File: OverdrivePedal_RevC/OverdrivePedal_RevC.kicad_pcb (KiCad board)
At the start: 2 copper layers, 42.5 x 30.5 mm, 58 parts, among them J1 AudioJack2-Connector, J2 Barrel_Jack, J3 Conn_01x05, J4 SW_SPST, J6 AudioJack2-Connector, U1 DG468DV_T1_E3, U10 PAM2812, U2 TL071, U3 TPS60400, U4 DG468DV_T1_E3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

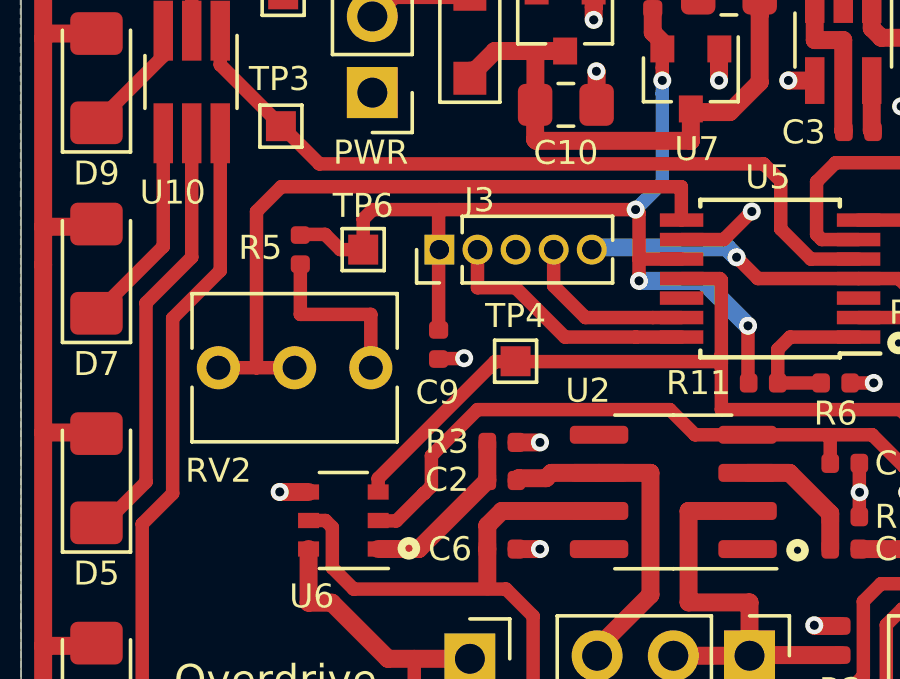
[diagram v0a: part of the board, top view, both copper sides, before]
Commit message: fixed wiring mistake on trim pot
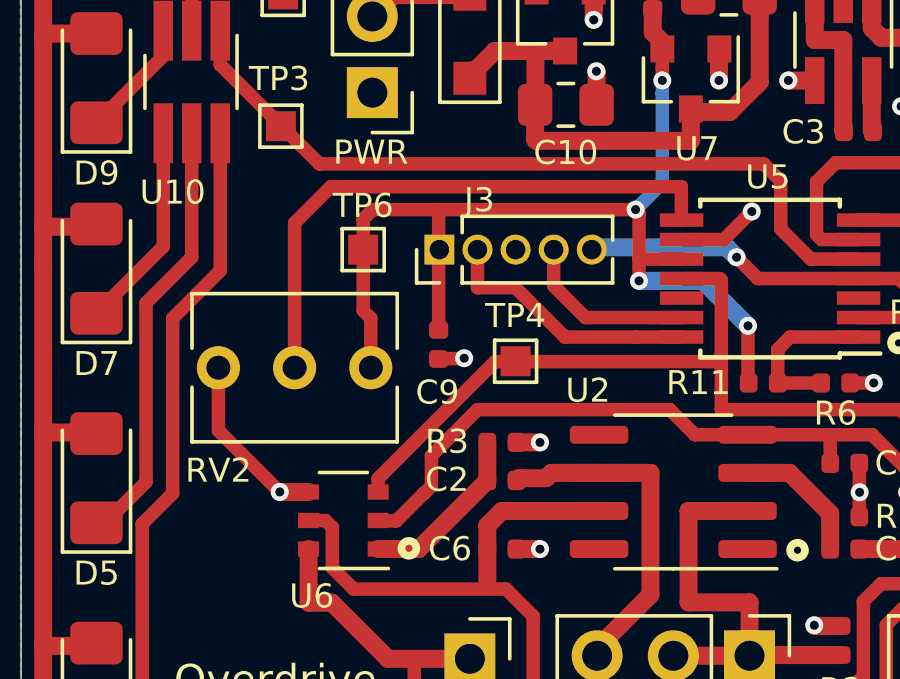
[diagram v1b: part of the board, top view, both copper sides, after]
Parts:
- removed R5: 1K, Resistor_SMD:R_0402_1005Metric
- C1, C2: value C -> 10uF
- R1: value 22M -> 10M
- R3: value 10K -> 10M
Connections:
- RV1 pad 3: Net-(C2-Pad2) -> Net-(R9-Pad2)
- RV2 pad 1: Net-(RV2-Pad1) -> GNDS
- RV2 pad 2: Net-(RV2-Pad1) -> Net-(RV2-Pad2)
- RV2 pad 3: Net-(R5-Pad1) -> +3V3
- U5 pad 8: Net-(RV2-Pad1) -> Net-(RV2-Pad2)
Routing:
- net Net-(RV2-Pad1): track 23.4 -> 0.00 mm
- net Net-(RV2-Pad2): track 0.00 -> 19.3 mm
- net Net-(R5-Pad1): track 5.80 -> 0.00 mm
- net GNDS: track 31.2 -> 36.2 mm
- net +3V3: track 33.5 -> 35.3 mm
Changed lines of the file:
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@@
     (thickness 1.6)
     (drawings 17)
-    (tracks 405)
+    (tracks 401)
     (zones 0)
-    (modules 58)
+    (modules 57)
     (nets 41)
   )
@@
   )
   (setup
-    (last_trace_width 0.25)
+    (last_trace_width 0.45)
     (user_trace_width 0.45)
     (user_trace_width 0.6)
@@
   (net 37 "Net-(U5-Pad12)")
   (net 38 "Net-(U5-Pad3)")
-  (net 39 "Net-(R5-Pad1)")
-  (net 40 "Net-(RV2-Pad1)")
+  (net 39 "Net-(R9-Pad2)")
+  (net 40 "Net-(RV2-Pad2)")
   (net_class Default "This is the default net class."
     (clearance 0.2)
@@
     (add_net "Net-(R11-Pad2)")
     (add_net "Net-(R2-Pad1)")
-    (add_net "Net-(R5-Pad1)")
-    (add_net "Net-(RV2-Pad1)")
+    (add_net "Net-(R9-Pad2)")
+    (add_net "Net-(RV2-Pad2)")
     (add_net "Net-(U2-Pad1)")
     (add_net "Net-(U2-Pad5)")
@@
     (fp_line (start 2.35 -0.76) (end 2.35 5.84) (layer F.Fab) (width 0.1))
     (pad 1 thru_hole circle (at 0 0 90) (size 1.44 1.44) (drill 0.8) (layers *.Cu *.Mask)
-      (net 40 "Net-(RV2-Pad1)"))
+      (net 1 GNDS))
     (pad 2 thru_hole circle (at 0 2.54 90) (size 1.44 1.44) (drill 0.8) (layers *.Cu *.Mask)
-      (net 40 "Net-(RV2-Pad1)"))
+      (net 40 "Net-(RV2-Pad2)"))
     (pad 3 thru_hole circle (at 0 5.08 90) (size 1.44 1.44) (drill 0.8) (layers *.Cu *.Mask)
-      (net 39 "Net-(R5-Pad1)"))
+      (net 20 +3V3))
     (model ${KISYS3DMOD}/Potentiometer_THT.3dshapes/Potentiometer_Vishay_T73XW_Horizontal.wrl
-      (at (xyz 0 0 0))
-      (scale (xyz 1 1 1))
-      (rotate (xyz 0 0 0))
-    )
-  )
-  (module Resistor_SMD:R_0402_1005Metric (layer F.Cu)
-    (at 132.5245 91.44 90)
-    (descr "Resistor SMD 0402 (1005 Metric), square (rectangular) end terminal, IPC_7351 nominal, (Body size source: http://www.tortai-tech.com/upload/download/2011102023233369053.pdf), generated with kicad-footprint-generator")
-    (tags resistor)
-    (attr smd)
-    (fp_text reference R5 (at 0.0635 -1.3335 180) (layer F.SilkS)
-      (effects (font (size 0.8 0.8) (thickness 0.15)))
-    )
-    (fp_text value 1K (at 0 1.17 90) (layer F.Fab)
-      (effects (font (size 1 1) (thickness 0.15)))
-    )
-    (fp_text user %R (at 0 0 90) (layer F.Fab)
-      (effects (font (size 1 1) (thickness 0.15)))
-    )
-    (fp_line (start 0.93 0.47) (end -0.93 0.47) (layer F.CrtYd) (width 0.05))
-    (fp_line (start 0.93 -0.47) (end 0.93 0.47) (layer F.CrtYd) (width 0.05))
-    (fp_line (start -0.93 -0.47) (end 0.93 -0.47) (layer F.CrtYd) (width 0.05))
-    (fp_line (start -0.93 0.47) (end -0.93 -0.47) (layer F.CrtYd) (width 0.05))
-    (fp_line (start 0.5 0.25) (end -0.5 0.25) (layer F.Fab) (width 0.1))
-    (fp_line (start 0.5 -0.25) (end 0.5 0.25) (layer F.Fab) (width 0.1))
-    (fp_line (start -0.5 -0.25) (end 0.5 -0.25) (layer F.Fab) (width 0.1))
-    (fp_line (start -0.5 0.25) (end -0.5 -0.25) (layer F.Fab) (width 0.1))
-    (pad 2 smd roundrect (at 0.485 0 90) (size 0.59 0.64) (layers F.Cu F.Paste F.Mask) (roundrect_rratio 0.25)
-      (net 20 +3V3))
-    (pad 1 smd roundrect (at -0.485 0 90) (size 0.59 0.64) (layers F.Cu F.Paste F.Mask) (roundrect_rratio 0.25)
-      (net 39 "Net-(R5-Pad1)"))
-    (model ${KISYS3DMOD}/Resistor_SMD.3dshapes/R_0402_1005Metric.wrl
       (at (xyz 0 0 0))
       (scale (xyz 1 1 1))
@@
       (net 1 GNDS))
     (pad 8 smd rect (at 2.95 1.95 180) (size 1.45 0.45) (layers F.Cu F.Paste F.Mask)
-      (net 40 "Net-(RV2-Pad1)"))
+      (net 40 "Net-(RV2-Pad2)"))
     (pad 7 smd rect (at -2.95 1.95 180) (size 1.45 0.45) (layers F.Cu F.Paste F.Mask)
       (net 31 /GPIO_EXTI4_BYPASS))
@@
     (fp_line (start -0.635 -1.27) (end 1.27 -1.27) (layer F.Fab) (width 0.1))
     (pad 3 thru_hole oval (at 0 5.08 270) (size 1.7 1.7) (drill 1) (layers *.Cu *.Mask)
-      (net 8 "Net-(C2-Pad2)"))
+      (net 39 "Net-(R9-Pad2)"))
     (pad 2 thru_hole oval (at 0 2.54 270) (size 1.7 1.7) (drill 1) (layers *.Cu *.Mask)
       (net 16 "Net-(R2-Pad1)"))
@@
       (effects (font (size 0.8 0.8) (thickness 0.15)))
     )
-    (fp_text value 10K (at 0 1.17) (layer F.Fab)
+    (fp_text value 10M (at 0 1.17) (layer F.Fab)
       (effects (font (size 1 1) (thickness 0.15)))
     )
@@
       (effects (font (size 0.8 0.8) (thickness 0.15)))
     )
-    (fp_text value 22M (at 0 1.17) (layer F.Fab)
+    (fp_text value 10M (at 0 1.17) (layer F.Fab)
       (effects (font (size 1 1) (thickness 0.15)))
     )
@@
       (effects (font (size 0.8 0.8) (thickness 0.15)))
     )
-    (fp_text value C (at 0 1.17) (layer F.Fab)
+    (fp_text value 10uF (at 0 1.17) (layer F.Fab)
       (effects (font (size 1 1) (thickness 0.15)))
     )
@@
       (effects (font (size 0.8 0.8) (thickness 0.15)))
     )
-    (fp_text value C (at 0 1.17) (layer F.Fab)
+    (fp_text value 10uF (at 0 1.17) (layer F.Fab)
       (effects (font (size 1 1) (thickness 0.15)))
     )
@@
   (via (at 137.9855 95.0595) (size 0.6) (drill 0.3) (layers F.Cu B.Cu) (net 1))
   (segment (start 137.1497 95.0722) (end 137.9728 95.0722) (width 0.45) (layer F.Cu) (net 1))
+  (segment (start 129.794 97.4725) (end 131.8387 99.5172) (width 0.45) (layer F.Cu) (net 1))
+  (segment (start 129.794 95.377) (end 129.794 97.4725) (width 0.45) (layer F.Cu) (net 1))
   (segment (start 141.374 84.843) (end 141.351 84.82) (width 0.6) (layer F.Cu) (net 2))
   (segment (start 139.0048 84.82) (end 141.351 84.82) (width 0.6) (layer F.Cu) (net 2))
@@
   (segment (start 147.447 93.98) (end 147.447 95.862) (width 0.45) (layer F.Cu) (net 20))
   (segment (start 137.414 91.186) (end 137.16 91.44) (width 0.45) (layer F.Cu) (net 20))
-  (segment (start 133.858 91.44) (end 133.35 90.932) (width 0.45) (layer F.Cu) (net 20))
-  (segment (start 134.62 91.44) (end 133.858 91.44) (width 0.45) (layer F.Cu) (net 20))
-  (segment (start 132.5475 90.932) (end 132.5245 90.955) (width 0.45) (layer F.Cu) (net 20))
-  (segment (start 133.35 90.932) (end 132.5475 90.932) (width 0.45) (layer F.Cu) (net 20))
   (segment (start 143.7005 90.1065) (end 144.5895 89.2175) (width 0.45) (layer B.Cu) (net 20))
   (segment (start 144.5895 86.225464) (end 144.5895 85.8012) (width 0.45) (layer B.Cu) (net 20))
@@
   (segment (start 137.1346 90.1319) (end 137.16 90.1065) (width 0.45) (layer F.Cu) (net 20))
   (segment (start 137.1346 94.1173) (end 137.1346 90.1319) (width 0.45) (layer F.Cu) (net 20))
+  (segment (start 134.874 95.377) (end 134.874 93.726) (width 0.45) (layer F.Cu) (net 20))
+  (segment (start 134.62 93.472) (end 134.62 91.44) (width 0.45) (layer F.Cu) (net 20))
+  (segment (start 134.874 93.726) (end 134.62 93.472) (width 0.45) (layer F.Cu) (net 20))
   (segment (start 161.4932 91.8607) (end 163.195 93.5625) (width 0.45) (layer F.Cu) (net 21))
   (segment (start 161.4932 90.043) (end 161.4932 91.8607) (width 0.45) (layer F.Cu) (net 21))
@@
   (segment (start 148.8498 94.3552) (end 148.44 94.765) (width 0.45) (layer F.Cu) (net 36))
   (segment (start 148.44 95.885) (end 149.883 95.885) (width 0.45) (layer F.Cu) (net 36))
-  (segment (start 134.874 95.377) (end 134.874 93.599) (width 0.45) (layer F.Cu) (net 39))
-  (segment (start 134.874 93.599) (end 132.5245 93.599) (width 0.45) (layer F.Cu) (net 39))
-  (segment (start 132.5245 93.599) (end 132.5245 91.925) (width 0.45) (layer F.Cu) (net 39))
-  (segment (start 131.064 95.377) (end 131.064 90.17) (width 0.45) (layer F.Cu) (net 40))
-  (segment (start 131.064 95.377) (end 129.794 95.377) (width 0.45) (layer F.Cu) (net 40))
-  (segment (start 132.334 95.377) (end 131.064 95.377) (width 0.45) (layer F.Cu) (net 40))
-  (segment (start 131.064 90.17) (end 131.8895 89.3445) (width 0.45) (layer F.Cu) (net 40))
-  (segment (start 131.8895 89.3445) (end 145.2245 89.3445) (width 0.45) (layer F.Cu) (net 40))
-  (segment (start 145.2245 90.4461) (end 145.2336 90.4552) (width 0.45) (layer F.Cu) (net 40))
-  (segment (start 145.2245 89.3445) (end 145.2245 90.4461) (width 0.45) (layer F.Cu) (net 40))
+  (segment (start 132.334 90.551) (end 132.334 95.377) (width 0.45) (layer F.Cu) (net 40))
+  (segment (start 133.5405 89.3445) (end 132.334 90.551) (width 0.45) (layer F.Cu) (net 40))
+  (segment (start 145.2245 89.3445) (end 133.5405 89.3445) (width 0.45) (layer F.Cu) (net 40))
+  (segment (start 145.2336 90.4552) (end 145.2245 90.4461) (width 0.45) (layer F.Cu) (net 40))
+  (segment (start 145.2245 90.4461) (end 145.2245 89.3445) (width 0.45) (layer F.Cu) (net 40))
   (zone (net 1) (net_name GNDS) (layer B.Cu) (hatch edge 0.508)
     (connect_pads yes (clearance 0.508))
